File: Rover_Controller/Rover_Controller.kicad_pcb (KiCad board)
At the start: 2 copper layers, 137.6 x 81.5 mm, 36 parts, among them Q1 S8050, SW1 SW_SPST, SW2 SW_SPST, SW3 SW_SPST, SW4 SW_SPST

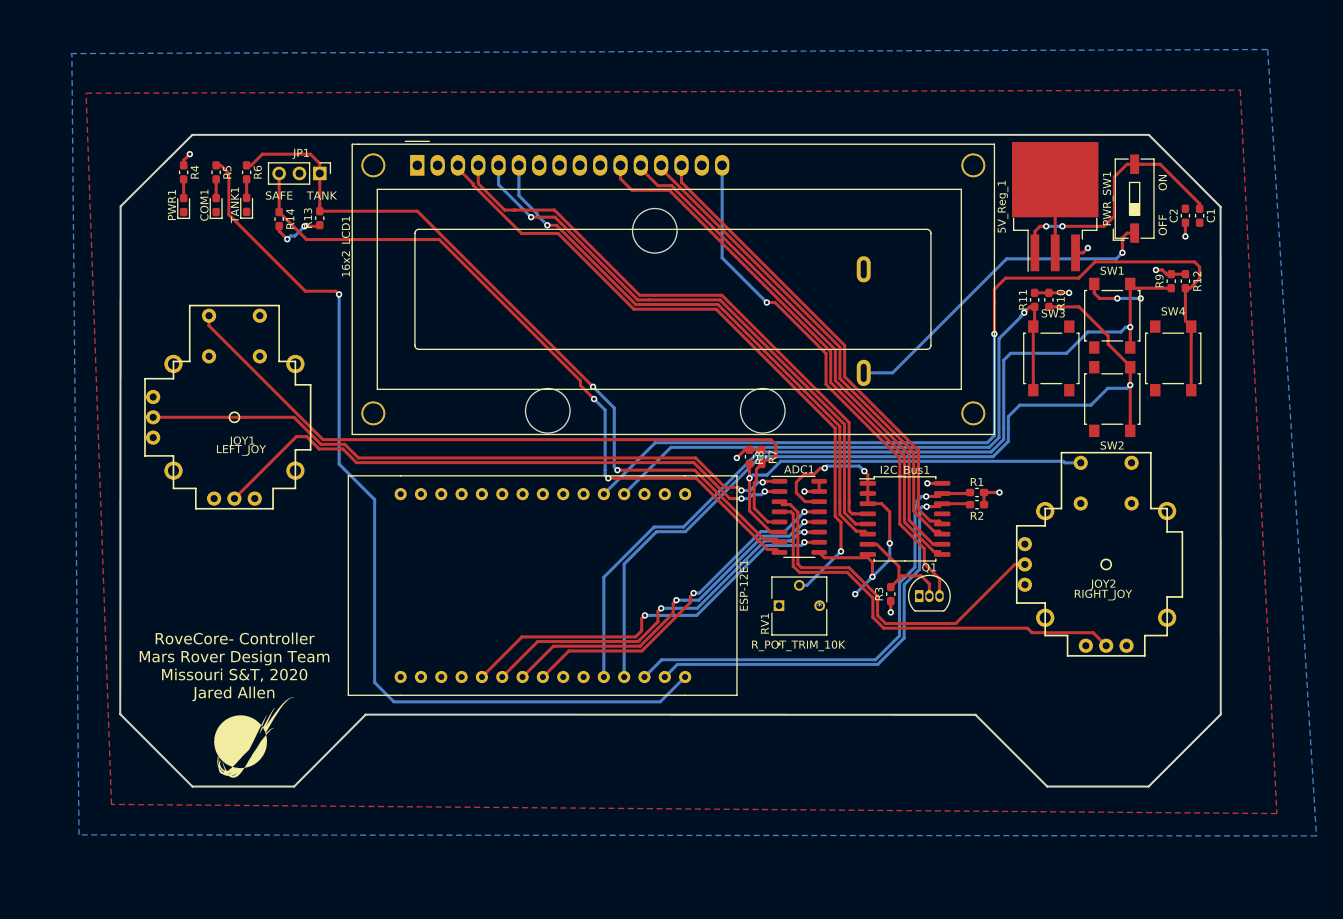
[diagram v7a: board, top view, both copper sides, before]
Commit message: Re-Traced Long Diagonal Traces
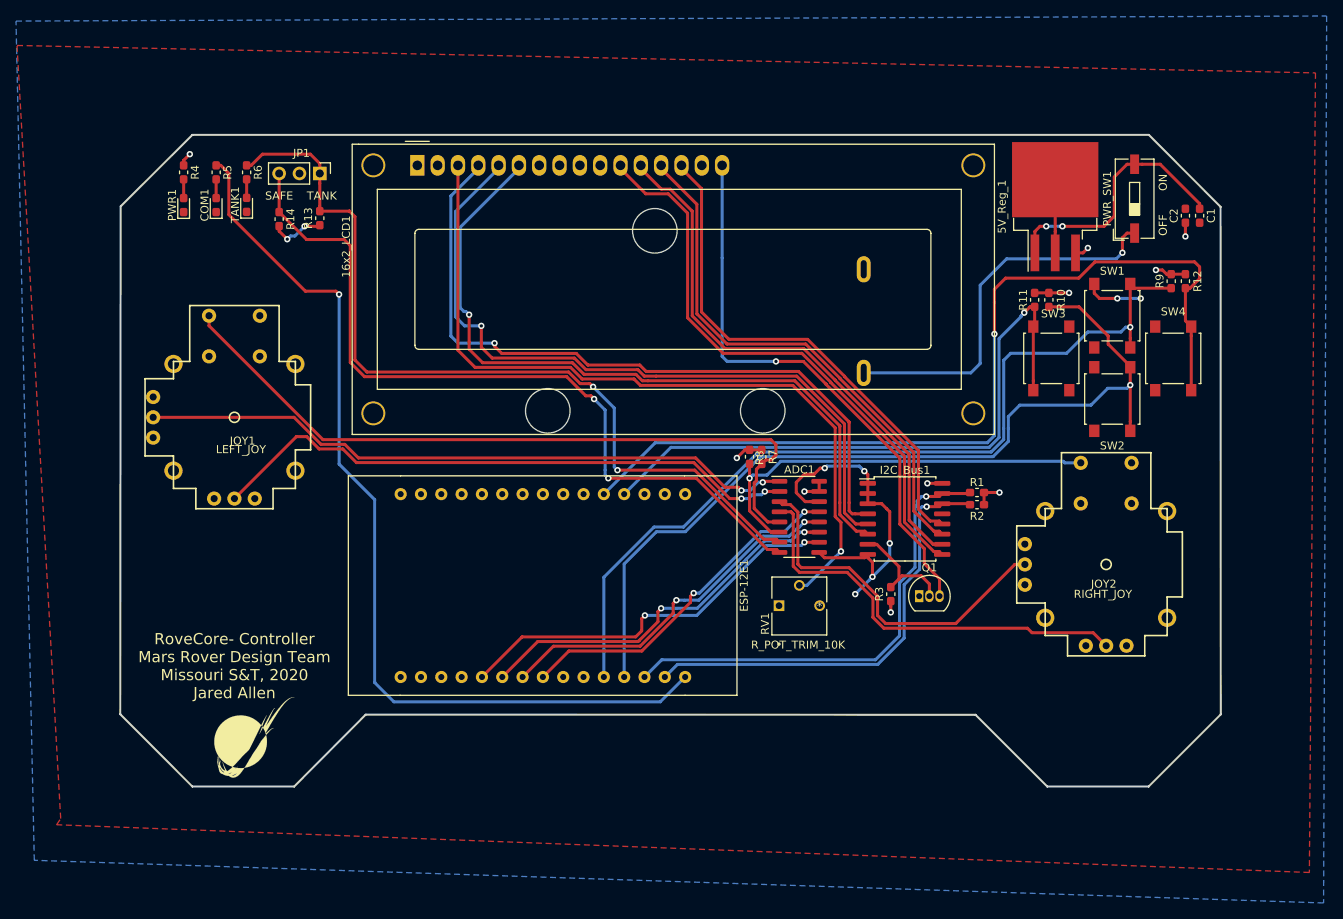
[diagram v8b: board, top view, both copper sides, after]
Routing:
- net Net-(16x2_LCD1-Pad6): track 71.9 -> 92.6 mm
- net Net-(16x2_LCD1-Pad5): track 73.0 -> 91.5 mm
- net Net-(16x2_LCD1-Pad4): track 74.7 -> 90.8 mm, vias 0 -> 1
- net V0: track 83.8 -> 97.4 mm
- net TankDrive: track 95.1 -> 105.6 mm
- net SafeDrive: track 90.1 -> 98.3 mm
- net Net-(16x2_LCD1-Pad13): track 61.0 -> 66.8 mm
- net Net-(16x2_LCD1-Pad14): track 59.0 -> 64.7 mm
- net Net-(BT1-Pad1): track 42.2 -> 47.9 mm
- net Net-(16x2_LCD1-Pad12): track 64.6 -> 70.0 mm
- net k: track 65.7 -> 70.7 mm
- net Net-(16x2_LCD1-Pad11): track 68.5 -> 73.1 mm
